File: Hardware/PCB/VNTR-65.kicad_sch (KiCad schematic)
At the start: 54 parts, among them J1 Conn_01x03_Pin, J2 USB_C_Receptacle, SW1 SW_Push, SW2 SW_Push, SW3 RotaryEncoder, U1 RP2350B, U2 NCP1117-3.3_SOT223, U3 W25Q128JVS, U4 USBLC6-2P6, U78 ER_OLEDM0.91_1x-I2C, Y1 Crystal_GND24

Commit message: Routed PCB
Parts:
- removed R17: 4.7k, Resistor_SMD:R_0603_1608Metric, symbol Device:R
- added R19: 4.7k, Resistor_SMD:R_0603_1608Metric, symbol Device:R
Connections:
- net +3V3 is gone; now on net +3.3V: RV1.1
- net +3.3V: now also R19.2
- net at U1.16 (GPIO16), U78.4 (SDA): now also R19.1
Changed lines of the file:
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@@
 	)
 	(junction
+		(at 262.89 97.79)
+		(diameter 0)
+		(color 0 0 0 0)
+	)
+	(junction
 		(at 213.36 17.78)
 		(diameter 0)
@@
 	)
 	(junction
-		(at 265.3575 97.79)
-		(diameter 0)
-		(color 0 0 0 0)
-	)
-	(junction
 		(at 167.64 34.29)
 		(diameter 0)
@@
 	(wire
 		(pts
-			(xy 266.7 97.79) (xy 265.3575 97.79)
+			(xy 262.89 97.79) (xy 266.7 97.79)
 		)
 		(stroke
@@
 	(wire
 		(pts
+			(xy 262.89 97.79) (xy 261.62 97.79)
+		)
+		(stroke
+			(width 0)
+			(type default)
+		)
+	)
+	(wire
+		(pts
 			(xy 173.99 90.17) (xy 173.99 123.19)
 		)
@@
 	(wire
 		(pts
-			(xy 265.3575 97.79) (xy 261.62 97.79)
-		)
-		(stroke
-			(width 0)
-			(type default)
-		)
-	)
-	(wire
-		(pts
 			(xy 245.11 29.21) (xy 245.11 36.83)
 		)
@@
 	)
 	(symbol
+		(lib_id "power:+3.3V")
+		(at 262.89 105.41 180)
+		(unit 1)
+		(body_style 1)
+		(exclude_from_sim no)
+		(in_bom yes)
+		(on_board yes)
+		(in_pos_files yes)
+		(dnp no)
+		(fields_autoplaced yes)
+		(property "Reference" "#PWR0186"
+			(at 262.89 101.6 0)
+			(hide yes)
+			(show_name no)
+			(do_not_autoplace no)
+			(effects
+				(font
+					(size 1.27 1.27)
+				)
+			)
+		)
+		(property "Value" "+3.3V"
+			(at 262.89 110.49 0)
+			(show_name no)
+			(do_not_autoplace no)
+			(effects
+				(font
+					(size 1.27 1.27)
+				)
+			)
+		)
+		(property "Footprint" ""
+			(at 262.89 105.41 0)
+			(hide yes)
+			(show_name no)
+			(do_not_autoplace no)
+			(effects
+				(font
+					(size 1.27 1.27)
+				)
+			)
+		)
+		(property "Datasheet" ""
+			(at 262.89 105.41 0)
+			(hide yes)
+			(show_name no)
+			(do_not_autoplace no)
+			(effects
+				(font
+					(size 1.27 1.27)
+				)
+			)
+		)
+		(property "Description" "Power symbol creates a global label with name \"+3.3V\""
+			(at 262.89 105.41 0)
+			(hide yes)
+			(show_name no)
+			(do_not_autoplace no)
+			(effects
+				(font
+					(size 1.27 1.27)
+				)
+			)
+		)
+		(pin "1"
+		)
+		(instances
+			(project "VNTR-65"
+				(path "/9381cecd-296d-4002-be35-b038a1e96b55"
+					(reference "#PWR0186")
+					(unit 1)
+				)
+			)
+		)
+	)
+	(symbol
 		(lib_id "Device:R")
 		(at 173.99 133.35 90)
@@
 	)
 	(symbol
+		(lib_id "Device:R")
+		(at 262.89 101.6 0)
+		(unit 1)
+		(body_style 1)
+		(exclude_from_sim no)
+		(in_bom yes)
+		(on_board yes)
+		(in_pos_files yes)
+		(dnp no)
+		(fields_autoplaced yes)
+		(property "Reference" "R19"
+			(at 265.5025 100.3299 0)
+			(show_name no)
+			(do_not_autoplace no)
+			(effects
+				(font
+					(size 1.27 1.27)
+				)
+				(justify left)
+			)
+		)
+		(property "Value" "4.7k"
+			(at 265.5025 102.8699 0)
+			(show_name no)
+			(do_not_autoplace no)
+			(effects
+				(font
+					(size 1.27 1.27)
+				)
+				(justify left)
+			)
+		)
+		(property "Footprint" "Resistor_SMD:R_0603_1608Metric"
+			(at 261.112 101.6 90)
+			(hide yes)
+			(show_name no)
+			(do_not_autoplace no)
+			(effects
+				(font
+					(size 1.27 1.27)
+				)
+			)
+		)
+		(property "Datasheet" ""
+			(at 262.89 101.6 0)
+			(hide yes)
+			(show_name no)
+			(do_not_autoplace no)
+			(effects
+				(font
+					(size 1.27 1.27)
+				)
+			)
+		)
+		(property "Description" "Resistor"
+			(at 262.89 101.6 0)
+			(hide yes)
+			(show_name no)
+			(do_not_autoplace no)
+			(effects
+				(font
+					(size 1.27 1.27)
+				)
+			)
+		)
+		(pin "2"
+		)
+		(pin "1"
+		)
+		(instances
+			(project "VNTR-65"
+				(path "/9381cecd-296d-4002-be35-b038a1e96b55"
+					(reference "R19")
+					(unit 1)
+				)
+			)
+		)
+	)
+	(symbol
 		(lib_id "power:GND")
 		(at 274.32 36.83 0)
@@
 			)
 		)
-		(property "Value" "+3V3"
+		(property "Value" "+3.3V"
 			(at 187.96 137.16 0)
 			(show_name no)
@@
 	(symbol
 		(lib_id "power:+3.3V")
-		(at 265.43 105.41 180)
-		(unit 1)
-		(body_style 1)
-		(exclude_from_sim no)
-		(in_bom yes)
-		(on_board yes)
-		(in_pos_files yes)
-		(dnp no)
-		(fields_autoplaced yes)
-		(property "Reference" "#PWR0186"
-			(at 265.43 101.6 0)
-			(hide yes)
-			(show_name no)
-			(do_not_autoplace no)
-			(effects
-				(font
-					(size 1.27 1.27)
-				)
-			)
-		)
-		(property "Value" "+3.3V"
-			(at 265.43 110.49 0)
-			(show_name no)
-			(do_not_autoplace no)
-			(effects
-				(font
-					(size 1.27 1.27)
-				)
-			)
-		)
-		(property "Footprint" ""
-			(at 265.43 105.41 0)
-			(hide yes)
-			(show_name no)
-			(do_not_autoplace no)
-			(effects
-				(font
-					(size 1.27 1.27)
-				)
-			)
-		)
-		(property "Datasheet" ""
-			(at 265.43 105.41 0)
-			(hide yes)
-			(show_name no)
-			(do_not_autoplace no)
-			(effects
-				(font
-					(size 1.27 1.27)
-				)
-			)
-		)
-		(property "Description" "Power symbol creates a global label with name \"+3.3V\""
-			(at 265.43 105.41 0)
-			(hide yes)
-			(show_name no)
-			(do_not_autoplace no)
-			(effects
-				(font
-					(size 1.27 1.27)
-				)
-			)
-		)
-		(pin "1"
-		)
-		(instances
-			(project "VNTR-65"
-				(path "/9381cecd-296d-4002-be35-b038a1e96b55"
-					(reference "#PWR0186")
-					(unit 1)
-				)
-			)
-		)
-	)
-	(symbol
-		(lib_id "power:+3.3V")
 		(at 96.52 44.45 0)
 		(unit 1)
@@
 					(unit 1)
 				)
-			)
-		)
-	)
-	(symbol
-		(lib_id "Device:R")
-		(at 265.3575 101.6 0)
-		(unit 1)
-		(body_style 1)
-		(exclude_from_sim no)
-		(in_bom yes)
-		(on_board yes)
-		(in_pos_files yes)
-		(dnp no)
-		(fields_autoplaced yes)
-		(property "Reference" "R17"
-			(at 267.97 100.3299 0)
-			(show_name no)
-			(do_not_autoplace no)
-			(effects
-				(font
-					(size 1.27 1.27)
-				)
-				(justify left)
-			)
-		)
-		(property "Value" "4.7k"
-			(at 267.97 102.8699 0)
-			(show_name no)
-			(do_not_autoplace no)
-			(effects
-				(font
-					(size 1.27 1.27)
-				)
-				(justify left)
-			)
-		)
-		(property "Footprint" "Resistor_SMD:R_0603_1608Metric"
-			(at 263.5795 101.6 90)
-			(hide yes)
-			(show_name no)
-			(do_not_autoplace no)
-			(effects
-				(font
-					(size 1.27 1.27)
-				)
-			)
-		)
-		(property "Datasheet" ""
-			(at 265.3575 101.6 0)
-			(hide yes)
-			(show_name no)
-			(do_not_autoplace no)
-			(effects
-				(font
-					(size 1.27 1.27)
-				)
-			)
-		)
-		(property "Description" "Resistor"
-			(at 265.3575 101.6 0)
-			(hide yes)
-			(show_name no)
-			(do_not_autoplace no)
-			(effects
-				(font
-					(size 1.27 1.27)
-				)
-			)
-		)
-		(pin "2"
-		)
-		(pin "1"
-		)
-		(instances
-			(project "VNTR-65"
-				(path "/9381cecd-296d-4002-be35-b038a1e96b55"
-					(reference "R17")
-					(unit 1)
-				)

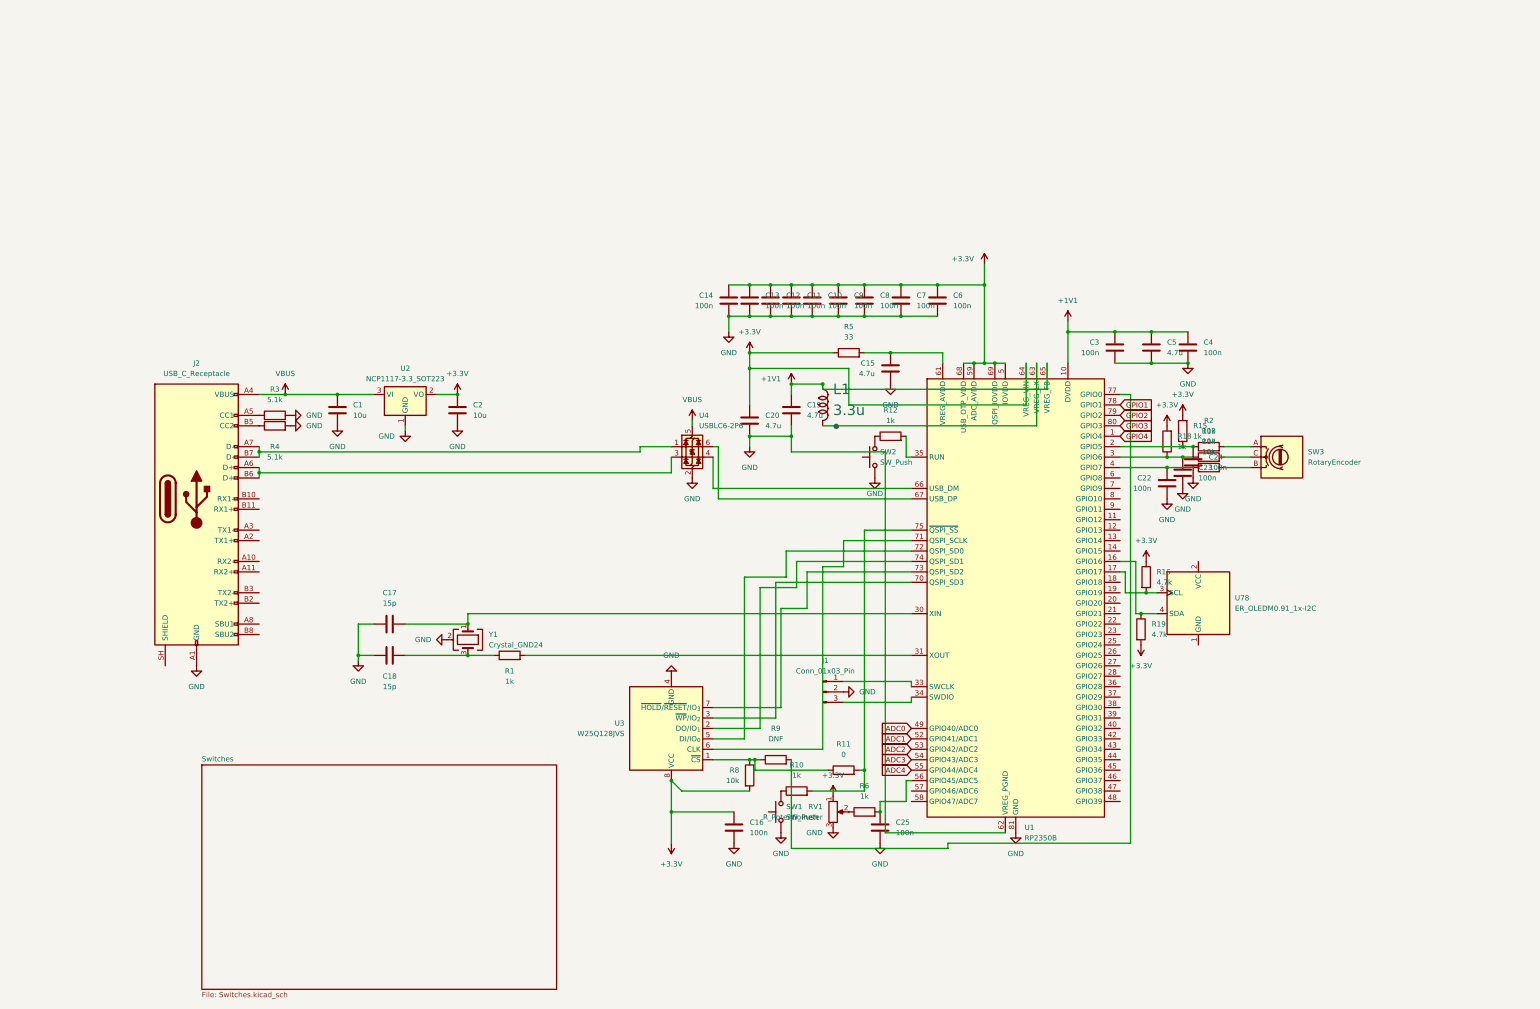
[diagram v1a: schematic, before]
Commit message: Updated to rp2350 to a version of the minimal base schematic
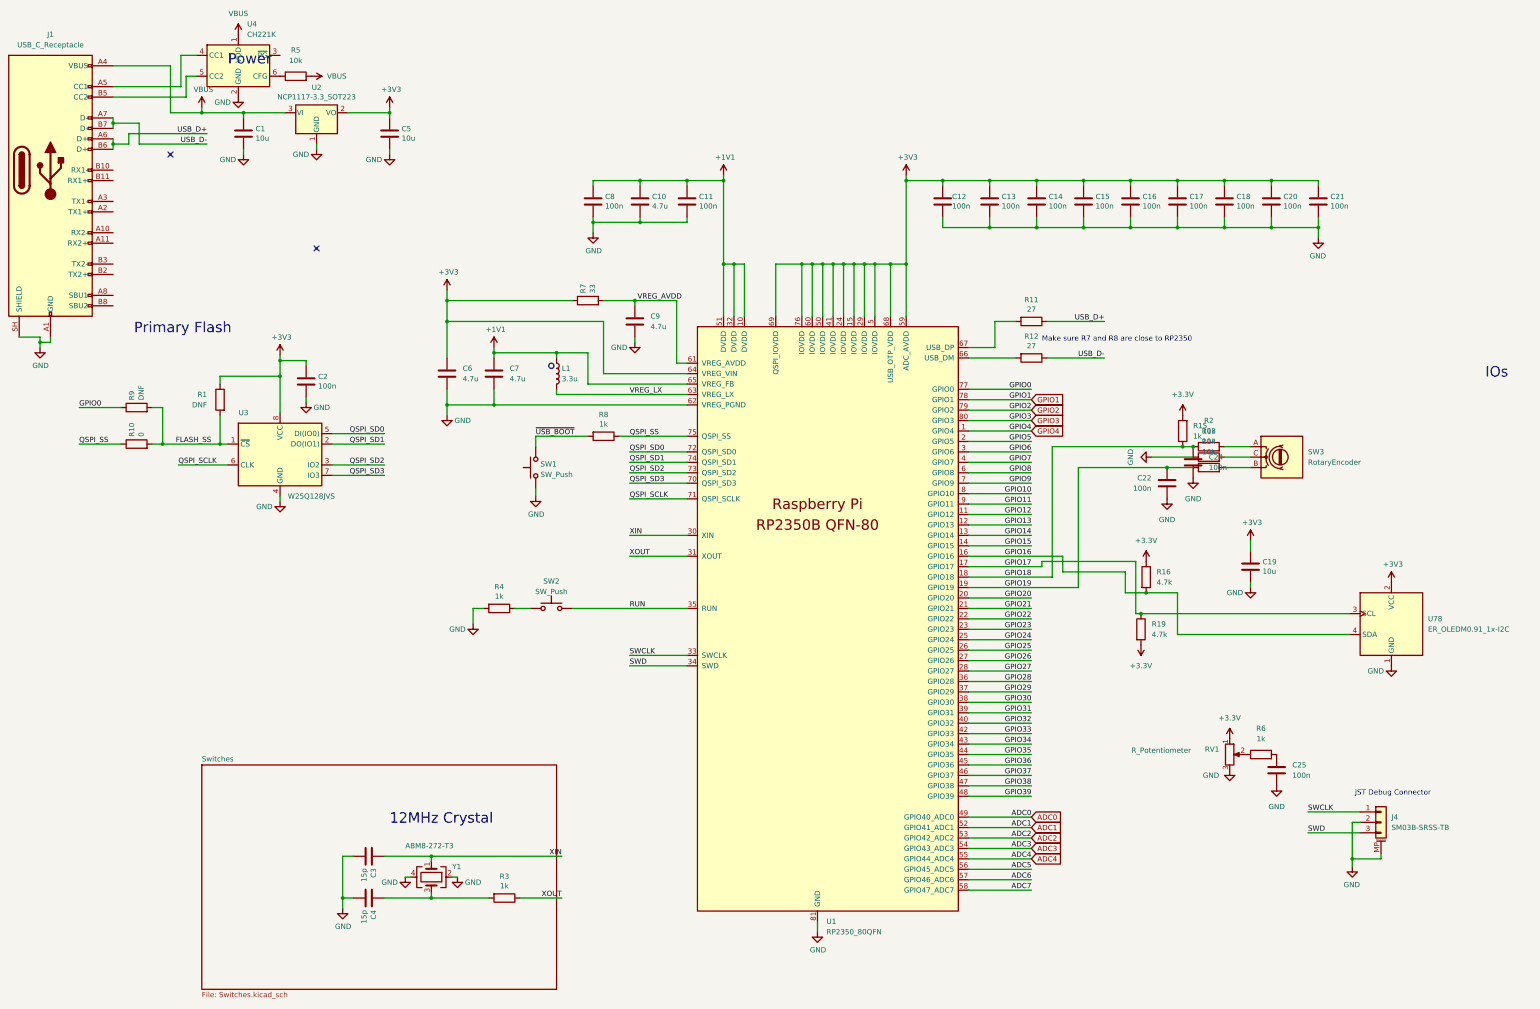
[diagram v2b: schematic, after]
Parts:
- removed C23: 100n, Capacitor_SMD:C_0603_1608Metric, symbol Device:C
- removed J1: Conn_01x03_Pin, Connector_PinHeader_1.00mm:PinHeader_1x03_P1.00mm_Vertical_SMD_Pin1Left, symbol Connector:Conn_01x03_Pin
- removed J2: USB_C_Receptacle, Connector_USB:USB_C_Receptacle_HRO_TYPE-C-31-M-12, symbol Connector:USB_C_Receptacle
- removed L1: 3.3u, Resistor_SMD:R_0603_1608Metric, symbol PCM_Generic:L,IEEE
- removed R18: 1k, Resistor_SMD:R_0603_1608Metric, symbol Device:R
- removed U1: RP2350B, Package_DFN_QFN:QFN-80-1EP_10x10mm_P0.4mm_EP3.4x3.4mm, symbol MCU_RaspberryPi:RP2350B
- removed U4: USBLC6-2P6, Package_TO_SOT_SMD:SOT-666, symbol Power_Protection:USBLC6-2P6
- added C21: 100n, Capacitor_SMD:C_0402_1005Metric, symbol Device:C
- added J1: USB_C_Receptacle, symbol Connector:USB_C_Receptacle
- added J4: SM03B-SRSS-TB, Connector_JST:JST_SH_SM03B-SRSS-TB_1x03-1MP_P1.00mm_Horizontal, symbol Connector_Generic_MountingPin:Conn_01x03_MountingPin
- added L1: 3.3u, RP2350_80QFN_minimal:L_pol_2016, symbol Device:L
- added R7: 33, Resistor_SMD:R_0402_1005Metric, symbol Device:R
- added U1: RP2350_80QFN, RP2350_80QFN_minimal:RP2350-QFN-80-1EP_10x10_P0.4mm_EP3.4x3.4mm_ThermalVias, symbol MCU_RaspberryPi_RP2350:RP2350_80QFN
- added U4: CH221K, Package_TO_SOT_SMD:SOT-23-6, symbol Interface_USB:CH221K
- C1: footprint Capacitor_SMD:C_0603_1608Metric -> Capacitor_SMD:C_0805_2012Metric
- C10, C9: value 100n -> 4.7u; footprint Capacitor_SMD:C_0603_1608Metric -> Capacitor_SMD:C_0402_1005Metric
- C11, C12, C13, C14, C16, C8: footprint Capacitor_SMD:C_0603_1608Metric -> Capacitor_SMD:C_0402_1005Metric
- C15, C20: value 4.7u -> 100n; footprint Capacitor_SMD:C_0603_1608Metric -> Capacitor_SMD:C_0402_1005Metric
- C17, C18: value 15p -> 100n; footprint Capacitor_SMD:C_0603_1608Metric -> Capacitor_SMD:C_0402_1005Metric
- C19, C5: value 4.7u -> 10u; footprint Capacitor_SMD:C_0603_1608Metric -> Capacitor_SMD:C_0805_2012Metric
- C2: value 10u -> 100n; footprint Capacitor_SMD:C_0603_1608Metric -> Capacitor_SMD:C_0402_1005Metric
- C3, C4: value 100n -> 15p; footprint Capacitor_SMD:C_0603_1608Metric -> Capacitor_SMD:C_0402_1005Metric
- C6, C7: value 100n -> 4.7u; footprint Capacitor_SMD:C_0603_1608Metric -> RP2350_80QFN_minimal:C_0402_1005Metric_small_pads
- R1: value 1k -> DNF; footprint Resistor_SMD:R_0603_1608Metric -> Resistor_SMD:R_0402_1005Metric
- R10: value 1k -> 0; footprint Resistor_SMD:R_0603_1608Metric -> Resistor_SMD:R_0402_1005Metric
- R11: value 0 -> 27; footprint Resistor_SMD:R_0603_1608Metric -> Resistor_SMD:R_0402_1005Metric
- R12: value 1k -> 27; footprint Resistor_SMD:R_0603_1608Metric -> Resistor_SMD:R_0402_1005Metric
- R3, R4: value 5.1k -> 1k; footprint Resistor_SMD:R_0603_1608Metric -> Resistor_SMD:R_0402_1005Metric
- R5: value 33 -> 10k; footprint Resistor_SMD:R_0603_1608Metric -> (none)
- R8: value 10k -> 1k; footprint Resistor_SMD:R_0603_1608Metric -> Resistor_SMD:R_0402_1005Metric
- R9: footprint Resistor_SMD:R_0603_1608Metric -> Resistor_SMD:R_0402_1005Metric
- SW1, SW2: footprint Button_Switch_THT:SW_PUSH_6mm -> Button_Switch_SMD:SW_Push_1P1T_NO_Vertical_Wuerth_434133025816
- U3: footprint Package_SO:SOIC-8_5.3x5.3mm_P1.27mm -> Package_SO:SOIC-8_5.23x5.23mm_P1.27mm
- Y1: value Crystal_GND24 -> ABM8-272-T3; private KLC_S4.1 -> (none)
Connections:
- net +1V1: now also C10.1, C11.1, C7.1, C8.1, L1.1, U1.10 (DVDD), U1.32 (DVDD), U1.51 (DVDD), U1.65 (VREG_FB); no longer C19.1, C3.1, C4.1, C5.1
- net +3.3V: no longer C10.1, C11.1, C12.1, C13.1, C14.1, C16.1, C2.1, C20.1, C6.1, C7.1, C8.1, C9.1, R5.1, R8.2, U2.2 (VO), U3.8 (VCC)
- net ADC0: now also U1.49 (GPIO40_ADC0)
- net ADC1: now also U1.52 (GPIO41_ADC1)
- net ADC2: now also U1.53 (GPIO42_ADC2)
- net ADC3: now also U1.54 (GPIO43_ADC3)
- net ADC4: now also U1.55 (GPIO44_ADC4)
- net GND: now also R13.1, U78.1 (GND), C21.2, J1.A1 (GND), J1.A12 (GND), J1.B1 (GND), J1.B12 (GND), J1.SH (SHIELD), J4.2 (Pin_2), J4.MP (MountPin), U1.62 (VREG_PGND), U1.81 (GND), U4.2 (GND); no longer R3.2, SW2.1
- net GPIO1: now also U1.78 (GPIO1)
- net GPIO2: now also U1.79 (GPIO2)
- net GPIO3: now also U1.80 (GPIO3)
- net GPIO4: now also U1.1 (GPIO4)
- net VBUS: now also R5.2, J1.A4 (VBUS), J1.A9 (VBUS), J1.B4 (VBUS), J1.B9 (VBUS), U4.1 (VDD)
- net at R4.1: now also SW2.1
- net FLASH_SS: now reaches R9.2
- net FLASH_SS: now also R1.2, R10.2, U3.1 (~{CS})
- net XOUT: now reaches R3.1
- net XOUT: now also U1.31 (XOUT)
- net QSPI_SS: now reaches R10.1
- net QSPI_SS: now also R8.1, U1.75 (QSPI_SS); no longer SW1.2
- net at R11.2: now also U1.67 (USB_DP); no longer R10.2
- net GPIO16: now reaches U78.4 (SDA)
- net GPIO16: now also R16.2, U1.16 (GPIO16); no longer R19.1
- net GPIO17: now reaches U78.3 (SCL)
- net GPIO17: now also R19.1, U1.17 (GPIO17); no longer R16.2
- net GPIO18: now reaches C24.2, R15.1, R2.1
- net GPIO18: now also U1.18 (GPIO18)
- net +3V3: now reaches C17.1
- net +3V3: now also C12.1, C13.1, C14.1, C15.1, C16.1, C18.1, C19.1, C2.1, C20.1, C5.1, C6.1, R1.1, U2.2 (VO), U3.8 (VCC), U78.2 (VCC), C21.1, R7.1, U1.15 (IOVDD), U1.24 (IOVDD), U1.29 (IOVDD), U1.41 (IOVDD), U1.5 (IOVDD), U1.50 (IOVDD), U1.59 (ADC_AVDD), U1.60 (IOVDD), U1.64 (VREG_VIN), U1.68 (USB_OTP_VDD), U1.69 (QSPI_IOVDD), U1.76 (IOVDD); no longer Y1.1
- net at R12.2: now also U1.66 (USB_DM)
- net GPIO19: now reaches C22.2, R14.1
- net GPIO19: now also U1.19 (GPIO19)
- net QSPI_SD2: now reaches U3.3 (IO2)
- net QSPI_SD2: now also U1.73 (QSPI_SD2)
- net QSPI_SCLK: now reaches U3.6 (CLK)
- net QSPI_SCLK: now also U1.71 (QSPI_SCLK)
- net QSPI_SD0: now reaches U3.5 (DI(IO0))
- net QSPI_SD0: now also U1.72 (QSPI_SD0)
- net QSPI_SD3: now reaches U3.7 (IO3)
- net QSPI_SD3: now also U1.70 (QSPI_SD3)
- net QSPI_SD1: now reaches U3.2 (DO(IO1))
- net QSPI_SD1: now also U1.74 (QSPI_SD1)
- net RUN: now reaches SW2.2
- net RUN: now also U1.35 (RUN); no longer R12.1
- new net: C4.1, R3.2, Y1.3
- new net: J1.A5 (CC1), U4.4 (CC1)
- new net: J1.B5 (CC2), U4.5 (CC2)
- new net: R5.1, U4.6 (CFG)
- new net ADC5: U1.56 (GPIO45_ADC5)
- new net ADC6: U1.57 (GPIO46_ADC6)
- new net ADC7: U1.58 (GPIO47_ADC7)
- new net GPIO0: R9.1, U1.77 (GPIO0)
- new net GPIO10: U1.8 (GPIO10)
- new net GPIO11: U1.9 (GPIO11)
- new net GPIO12: U1.11 (GPIO12)
- new net GPIO13: U1.12 (GPIO13)
- new net GPIO14: U1.13 (GPIO14)
- new net GPIO15: U1.14 (GPIO15)
- new net GPIO20: U1.20 (GPIO20)
- new net GPIO21: U1.21 (GPIO21)
- new net GPIO22: U1.22 (GPIO22)
- new net GPIO23: U1.23 (GPIO23)
- new net GPIO24: U1.25 (GPIO24)
- new net GPIO25: U1.26 (GPIO25)
- new net GPIO26: U1.27 (GPIO26)
- new net GPIO27: U1.28 (GPIO27)
- new net GPIO28: U1.36 (GPIO28)
- new net GPIO29: U1.37 (GPIO29)
- new net GPIO30: U1.38 (GPIO30)
- new net GPIO31: U1.39 (GPIO31)
- new net GPIO32: U1.40 (GPIO32)
- new net GPIO33: U1.42 (GPIO33)
- new net GPIO34: U1.43 (GPIO34)
- new net GPIO35: U1.44 (GPIO35)
- new net GPIO36: U1.45 (GPIO36)
- new net GPIO37: U1.46 (GPIO37)
- new net GPIO38: U1.47 (GPIO38)
- new net GPIO39: U1.48 (GPIO39)
- new net GPIO5: U1.2 (GPIO5)
- new net GPIO6: U1.3 (GPIO6)
- new net GPIO7: U1.4 (GPIO7)
- new net GPIO8: U1.6 (GPIO8)
- new net GPIO9: U1.7 (GPIO9)
- new net SWCLK: J4.1 (Pin_1), U1.33 (SWCLK)
- new net SWD: J4.3 (Pin_3), U1.34 (SWD)
- new net USB_D+: J1.A6 (D+), J1.B6 (D+), R11.1
- new net USB_D-: J1.A7 (D-), J1.B7 (D-), R12.1
- new net VREG_AVDD: C9.1, R7.2, U1.61 (VREG_AVDD)
- new net VREG_LX: L1.2, U1.63 (VREG_LX)
- new net XIN: C3.1, U1.30 (XIN), Y1.1
- new net ~{USB_BOOT}: R8.2, SW1.2
- no-connect marks 0 -> 2
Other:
- note added: "12MHz Crystal"
- note added: "IOs"
- note added: "JST Debug Connector"
- note added: "Make sure R7 and R8 are close to RP2350"
- note added: "Power"
- note added: "Primary Flash"
- moved on the sheet: C25, R6, RV1, U78

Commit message: Connected everything with the new rp2350 setup
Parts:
- J1: footprint (none) -> Connector_USB:USB_C_Receptacle_Amphenol_12401610E4-2A
- R5: footprint (none) -> Resistor_SMD:R_0402_1005Metric
- RV1: footprint (none) -> PCM_Potentiometer_THT_AKL:Potentiometer_Bourns_PTA6043_Single_Slide
- SW3: footprint (none) -> Rotary_Encoder:RotaryEncoder_Alps_EC11E-Switch_Vertical_H20mm
- U1: footprint RP2350_80QFN_minimal:RP2350-QFN-80-1EP_10x10_P0.4mm_EP3.4x3.4mm_ThermalVias -> Package_DFN_QFN:QFN-80-1EP_10x10mm_P0.4mm_EP3.4x3.4mm
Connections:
- net GPIO26: now also C25.2, R6.2
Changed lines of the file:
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@@
 	)
 	(junction
+		(at 295.91 132.08)
+		(diameter 0)
+		(color 0 0 0 0)
+	)
+	(junction
 		(at 68.58 167.005)
 		(diameter 0)
@@
 	(wire
 		(pts
+			(xy 295.91 132.08) (xy 295.91 109.22)
+		)
+		(stroke
+			(width 0)
+			(type default)
+		)
+	)
+	(wire
+		(pts
 			(xy 173.99 25.4) (xy 173.99 12.7)
 		)
@@
 	(wire
 		(pts
-			(xy 220.98 109.22) (xy 236.22 109.22)
+			(xy 220.98 109.22) (xy 295.91 109.22)
 		)
 		(stroke
@@
 			)
 		)
-		(property "Footprint" ""
+		(property "Footprint" "Rotary_Encoder:RotaryEncoder_Alps_EC11E-Switch_Vertical_H20mm"
 			(at 293.37 55.626 0)
 			(hide yes)
@@
 			)
 		)
-		(property "Footprint" "RP2350_80QFN_minimal:RP2350-QFN-80-1EP_10x10_P0.4mm_EP3.4x3.4mm_ThermalVias"
+		(property "Footprint" "Package_DFN_QFN:QFN-80-1EP_10x10mm_P0.4mm_EP3.4x3.4mm"
 			(at 165.1 76.2 0)
 			(hide yes)
@@
 			)
 		)
-		(property "Footprint" ""
+		(property "Footprint" "Connector_USB:USB_C_Receptacle_Amphenol_12401610E4-2A"
 			(at 1.27 -10.16 0)
 			(hide yes)
@@
 			)
 		)
-		(property "Footprint" ""
+		(property "Footprint" "Resistor_SMD:R_0402_1005Metric"
 			(at 57.15 -31.242 90)
 			(hide yes)
@@
 			)
 		)
-		(property "Footprint" ""
+		(property "Footprint" "PCM_Potentiometer_THT_AKL:Potentiometer_Bourns_PTA6043_Single_Slide"
 			(at 284.48 132.08 0)
 			(hide yes)

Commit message: Refined the pcb design overall
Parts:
- removed R1, R9: DNF, Resistor_SMD:R_0402_1005Metric, symbol Device:R
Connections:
- net +3.3V is gone; now on net +3V3: R15.2, R16.1, R19.2, RV1.1
